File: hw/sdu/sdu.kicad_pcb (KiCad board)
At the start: 2 copper layers, 54 parts, among them J1 INTERFACE, J2 SWD, Q1 BC847, Q2 BC857, Q3 BC857, Q4 BC857, Q5 BC847, Q6 BC847, Q7 BC847, U1 TS1117BCW33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

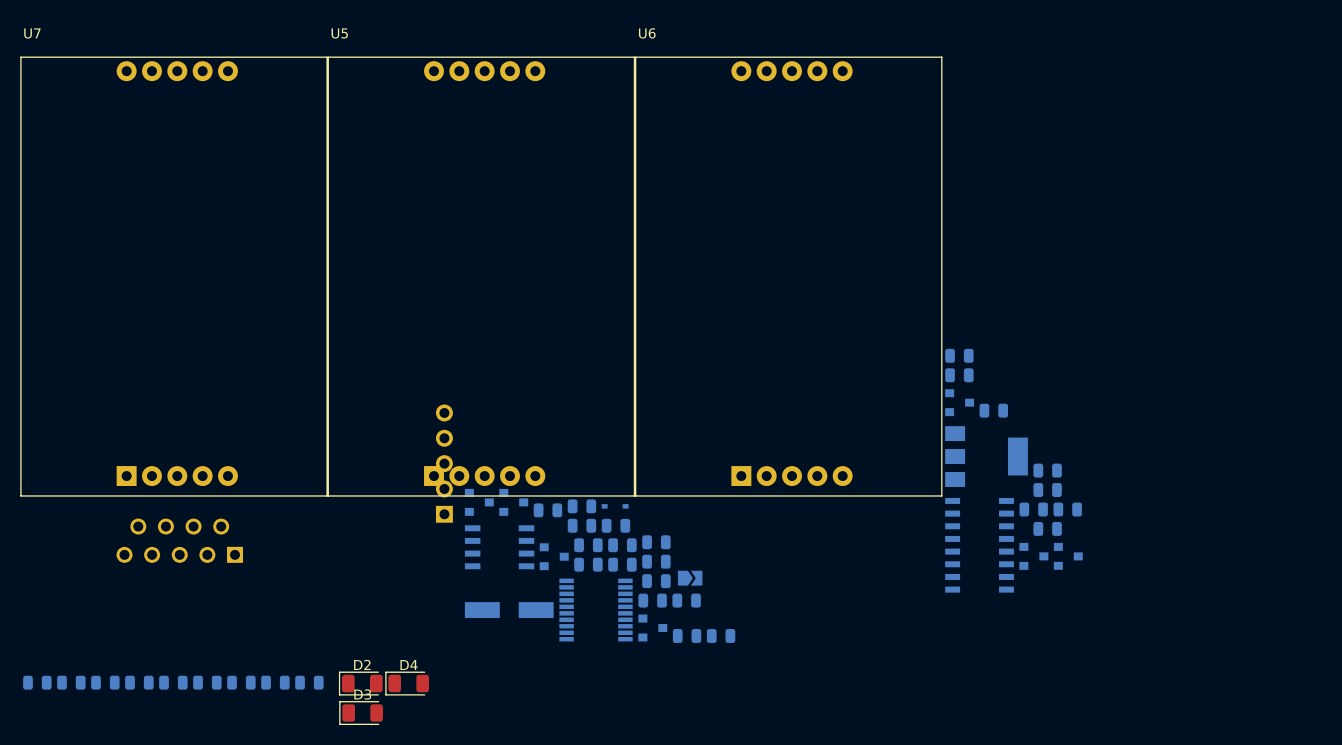
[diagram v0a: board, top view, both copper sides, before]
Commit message: Added HMI and SDU boards
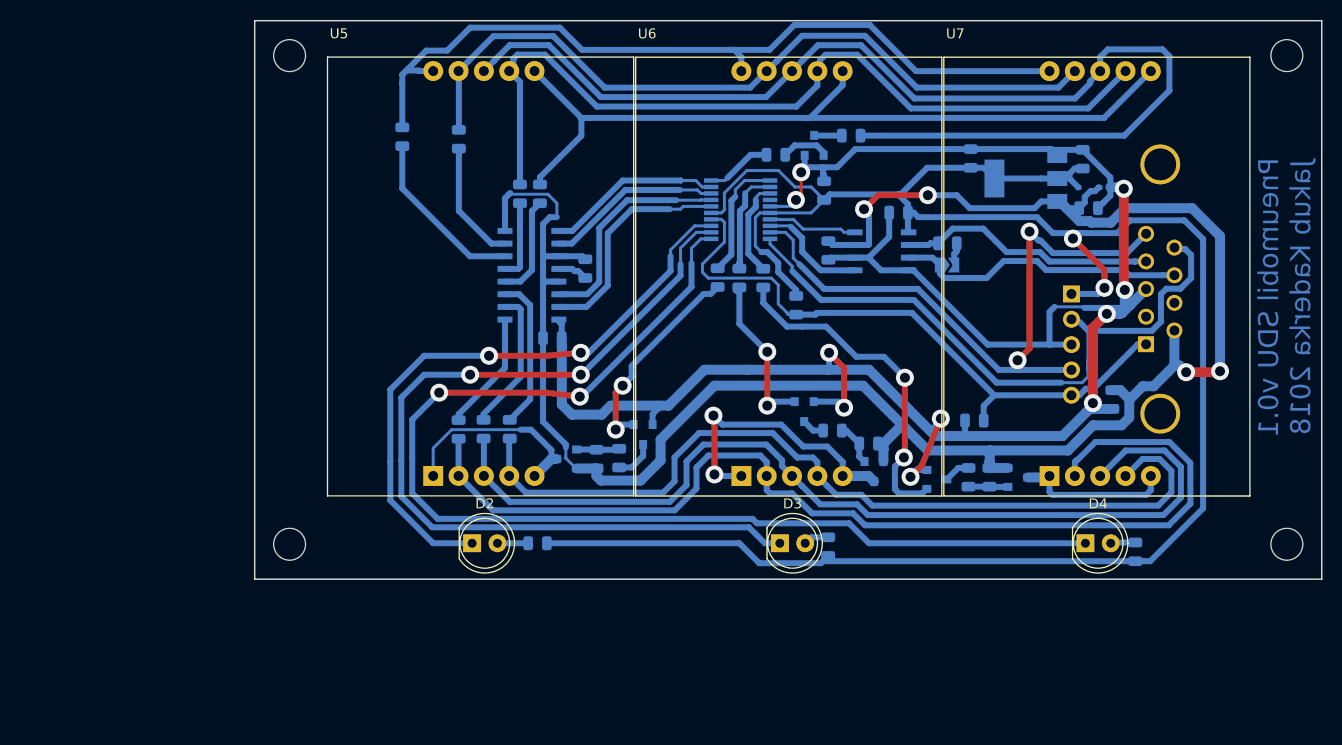
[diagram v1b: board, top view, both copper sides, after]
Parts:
- added REF**: MountingHole_3.2mm_M3, MountingHole:MountingHole_3.2mm_M3, F.Cu at (206.0, 69.3)
- added REF**: MountingHole_3.2mm_M3, MountingHole:MountingHole_3.2mm_M3, F.Cu at (106.0, 69.3)
- added REF**: MountingHole_3.2mm_M3, MountingHole:MountingHole_3.2mm_M3, F.Cu at (106.0, 118.3)
- added REF**: MountingHole_3.2mm_M3, MountingHole:MountingHole_3.2mm_M3, F.Cu at (206.0, 118.3)
- C1: value 50u -> 10u; footprint Capacitor_SMD:CP_Elec_6.3x7.7 -> Capacitor_SMD:C_0805_2012Metric
- D2, D3, D4: footprint LED_SMD:LED_1206_3216Metric -> LED_THT:LED_D5.0mm
- J1: footprint Connector_Dsub:DSUB-9_Female_Vertical_P2.77x2.84mm -> Connector_Dsub:DSUB-9_Female_Vertical_P2.77x2.84mm_MountingHoles
- J2: footprint Connector_PinSocket_2.54mm:PinSocket_1x05_P2.54mm_Horizontal -> Connector_PinHeader_2.54mm:PinHeader_1x05_P2.54mm_Horizontal
- moved C5 117.2 mm to (185.5, 79.7), turned to 90 degrees
- moved C6 104.4 mm to (174.3, 79.6), turned to 90 degrees
- moved R4 104.1 mm to (190.8, 119.1), turned to 270 degrees
- moved J1 93.8 mm to (191.9, 98.2), turned to 270 degrees
- moved U7 92.5 mm to (182.2, 111.5)
- moved C7 87.8 mm to (174.7, 105.9), turned to 180 degrees
- moved R1 83.4 mm to (172.0, 88.1), turned to 180 degrees
- moved C8 81.8 mm to (159.6, 82.8), turned to 270 degrees
- moved D4 69.3 mm to (185.8, 118.2)
- moved J2 66.6 mm to (184.4, 93.2), turned to 180 degrees
- moved C1 64.1 mm to (188.5, 103.8), turned to 270 degrees
- moved D1 57.3 mm to (186.2, 82.5), turned to 180 degrees
- moved R14 54.6 mm to (117.3, 77.4), turned to 270 degrees
- moved Q4 54.1 mm to (179.0, 111.6)
- moved R3 53.8 mm to (160.0, 118.5), turned to 270 degrees
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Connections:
- net Net-(U3-Pad6) renamed /A
- net Net-(U3-Pad8) renamed /C
- U3 pad 14: Net-(D3-Pad1) -> (no net)
- U3 pad 2: (no net) -> Net-(D3-Pad1)
- U3 pad 7: Net-(U3-Pad7) -> /D
- U3 pad 9: Net-(U3-Pad9) -> /B
- U4 pad 1: Net-(U3-Pad7) -> /B
- U4 pad 6: Net-(U3-Pad9) -> /D
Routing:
- net GND: track 0.00 -> 215.0 mm, vias 0 -> 10
- net +3V3: track 0.00 -> 206.3 mm, vias 0 -> 2
- net +5V: track 0.00 -> 204.2 mm, vias 0 -> 4
- net Net-(D4-Pad1): track 0.00 -> 116.9 mm, vias 0 -> 2
- net Net-(R15-Pad1): track 0.00 -> 115.9 mm
- net Net-(R12-Pad1): track 0.00 -> 106.3 mm
- net Net-(R11-Pad1): track 0.00 -> 95.4 mm
- net Net-(D3-Pad1): track 0.00 -> 89.4 mm, vias 0 -> 2
- net Net-(R10-Pad1): track 0.00 -> 87.1 mm
- net Net-(R8-Pad1): track 0.00 -> 84.2 mm
- net Net-(R14-Pad1): track 0.00 -> 81.5 mm
- net Net-(R9-Pad1): track 0.00 -> 80.6 mm
- net Net-(R13-Pad1): track 0.00 -> 76.3 mm
- net /SWDIO: track 0.00 -> 64.8 mm, vias 0 -> 2
- net /SWCLK: track 0.00 -> 63.9 mm
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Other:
- board outline added: 107 x 56 mm
- net class Default: clearance 0.2 -> 0.25; trace_width 0.25 -> 0.3
- rule trace_clearance: 0.2 -> 0.25
- rule trace_min: 0.2 -> 0.3
- board text added: "BUT FEEC BUT FME"
- board text added: "Pneumobil SDU v0.1 Jakub Kaderka 2018"

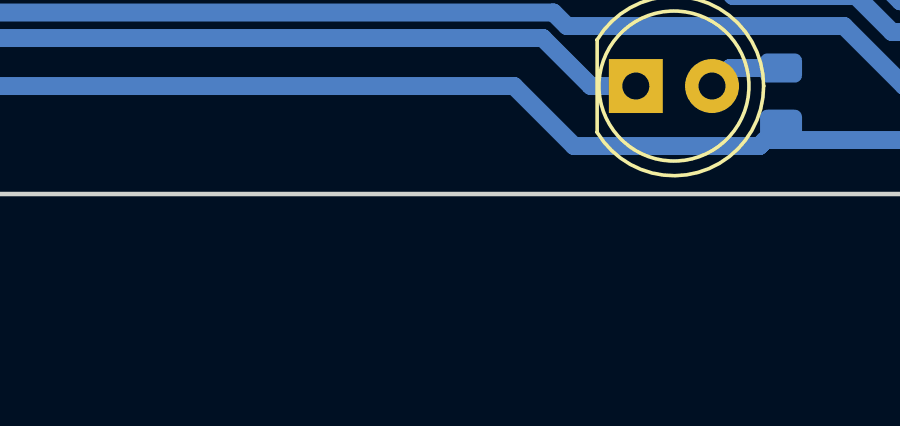
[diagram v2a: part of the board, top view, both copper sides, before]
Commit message: Added crystal for all can equipped boards
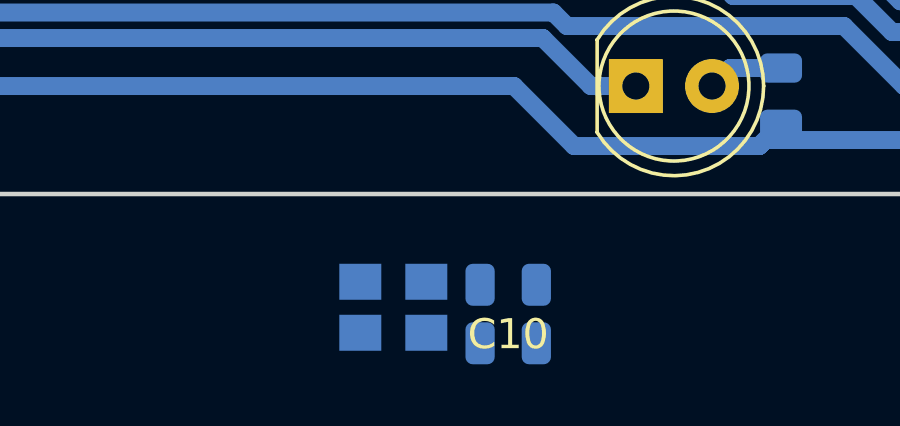
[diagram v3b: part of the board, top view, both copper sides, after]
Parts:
- added C10: 3p9, Capacitor_SMD:C_0805_2012Metric, B.Cu at (150.9, 124.8)
- added C11: 3p9, Capacitor_SMD:C_0805_2012Metric, B.Cu at (150.9, 126.8)
- added Y1: MCSJK-7U-16.00, Crystal:Crystal_SMD_3225-4Pin_3.2x2.5mm, B.Cu at (147.1, 125.6)
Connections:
- D2 pad 1: Net-(D2-Pad1) -> /LED1
- D3 pad 1: Net-(D3-Pad1) -> /LED2
- D4 pad 1: Net-(D4-Pad1) -> /LED3
- Q1 pad 3: Net-(Q1-Pad3) -> (no net)
- R15 pad 2: Net-(Q1-Pad3) -> GND
- R7 pad 2: Net-(R7-Pad2) -> (no net)
- U3 pad 1: Net-(D4-Pad1) -> /LED2
- U3 pad 10: Net-(R7-Pad2) -> /LED3
- U3 pad 14: (no net) -> /LED1
- U3 pad 2: Net-(D3-Pad1) -> Net-(C10-Pad1)
- U3 pad 3: Net-(D2-Pad1) -> Net-(C11-Pad1)
- U5 pad 8: Net-(R15-Pad1) -> (no net)
- U7 pad 8: Net-(R15-Pad1) -> (no net)
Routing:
- net Net-(R7-Pad2): track 6.62 -> 0.00 mm
- net /LED3: track 0.00 -> 6.62 mm
- net Net-(Q1-Pad3): track 2.79 -> 0.00 mm
- net GND: track 215.0 -> 217.8 mm

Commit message: Updated SDU board
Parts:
- removed Q1: BC847, Package_TO_SOT_SMD:SOT-23
- removed R7: 10k, Resistor_SMD:R_0805_2012Metric
- moved C11 40.2 mm to (140.4, 88.0), turned to 270 degrees
- moved Y1 37.8 mm to (143.5, 88.0), turned to 180 degrees
- moved C10 34.9 mm to (143.3, 90.8), turned to 180 degrees
- moved C7 32.7 mm to (154.5, 80.2), turned to 0 degrees
- moved JP1 30.7 mm to (202.6, 91.8)
- moved R1 30.6 mm to (202.5, 89.5)
- moved R5 15.3 mm to (151.0, 80.2), turned to 0 degrees
- moved C1 15.0 mm to (201.4, 96.0), turned to 90 degrees
- moved R15 7.50 mm to (156.2, 72.9), turned to 0 degrees
- moved R23 5.62 mm to (171.0, 109.3)
- moved Q4 5.62 mm to (173.9, 109.4)
- moved Q7 5.62 mm to (165.8, 109.6)
- moved R24 5.62 mm to (168.9, 109.3)
- moved R8 5.36 mm to (128.0, 77.9)
- moved R9 5.29 mm to (130.6, 77.9)
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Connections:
- U3 pad 10: /LED3 -> /LED1
- U3 pad 14: /LED1 -> /LED3
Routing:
- net GND: track 217.8 -> 63.6 mm, vias 10 -> 11
- net Net-(D4-Pad1): track 116.9 -> 0.00 mm, vias 2 -> 0
- net Net-(R15-Pad1): track 115.9 -> 2.52 mm
- net Net-(D3-Pad1): track 89.4 -> 0.00 mm, vias 2 -> 0
- net /LED1: track 0.00 -> 63.8 mm, vias 0 -> 2
- net Net-(D2-Pad1): track 61.9 -> 0.00 mm, vias 2 -> 0
- net /LED3: track 6.62 -> 64.6 mm, vias 0 -> 2
- net /LED2: track 0.00 -> 43.0 mm, vias 0 -> 2
- net Net-(R12-Pad1): track 106.3 -> 76.9 mm
- net Net-(R11-Pad1): track 95.4 -> 74.8 mm
- net Net-(Q4-Pad3): track 15.7 -> 35.1 mm
- net Net-(R10-Pad1): track 87.1 -> 74.3 mm
- net Net-(Q3-Pad3): track 28.4 -> 16.9 mm, vias 2 -> 0
- net /SWCLK: track 63.9 -> 54.3 mm, vias 0 -> 1
- net Net-(C11-Pad1): track 0.00 -> 9.30 mm
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- added copper zone on F.Cu, net GND
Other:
- board text added: "Pneumobil SDU v0.2 Jakub Kaderka 2019"
- board text removed: "Pneumobil SDU v0.1 Jakub Kaderka 2018"
